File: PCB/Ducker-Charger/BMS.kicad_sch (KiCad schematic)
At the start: 39 parts, among them IC3 BQ34Z100PWR-R2, Q12 BC846, Q13 NCE3080K, Q14 NCE3080K, U8 BQ7791500PWR

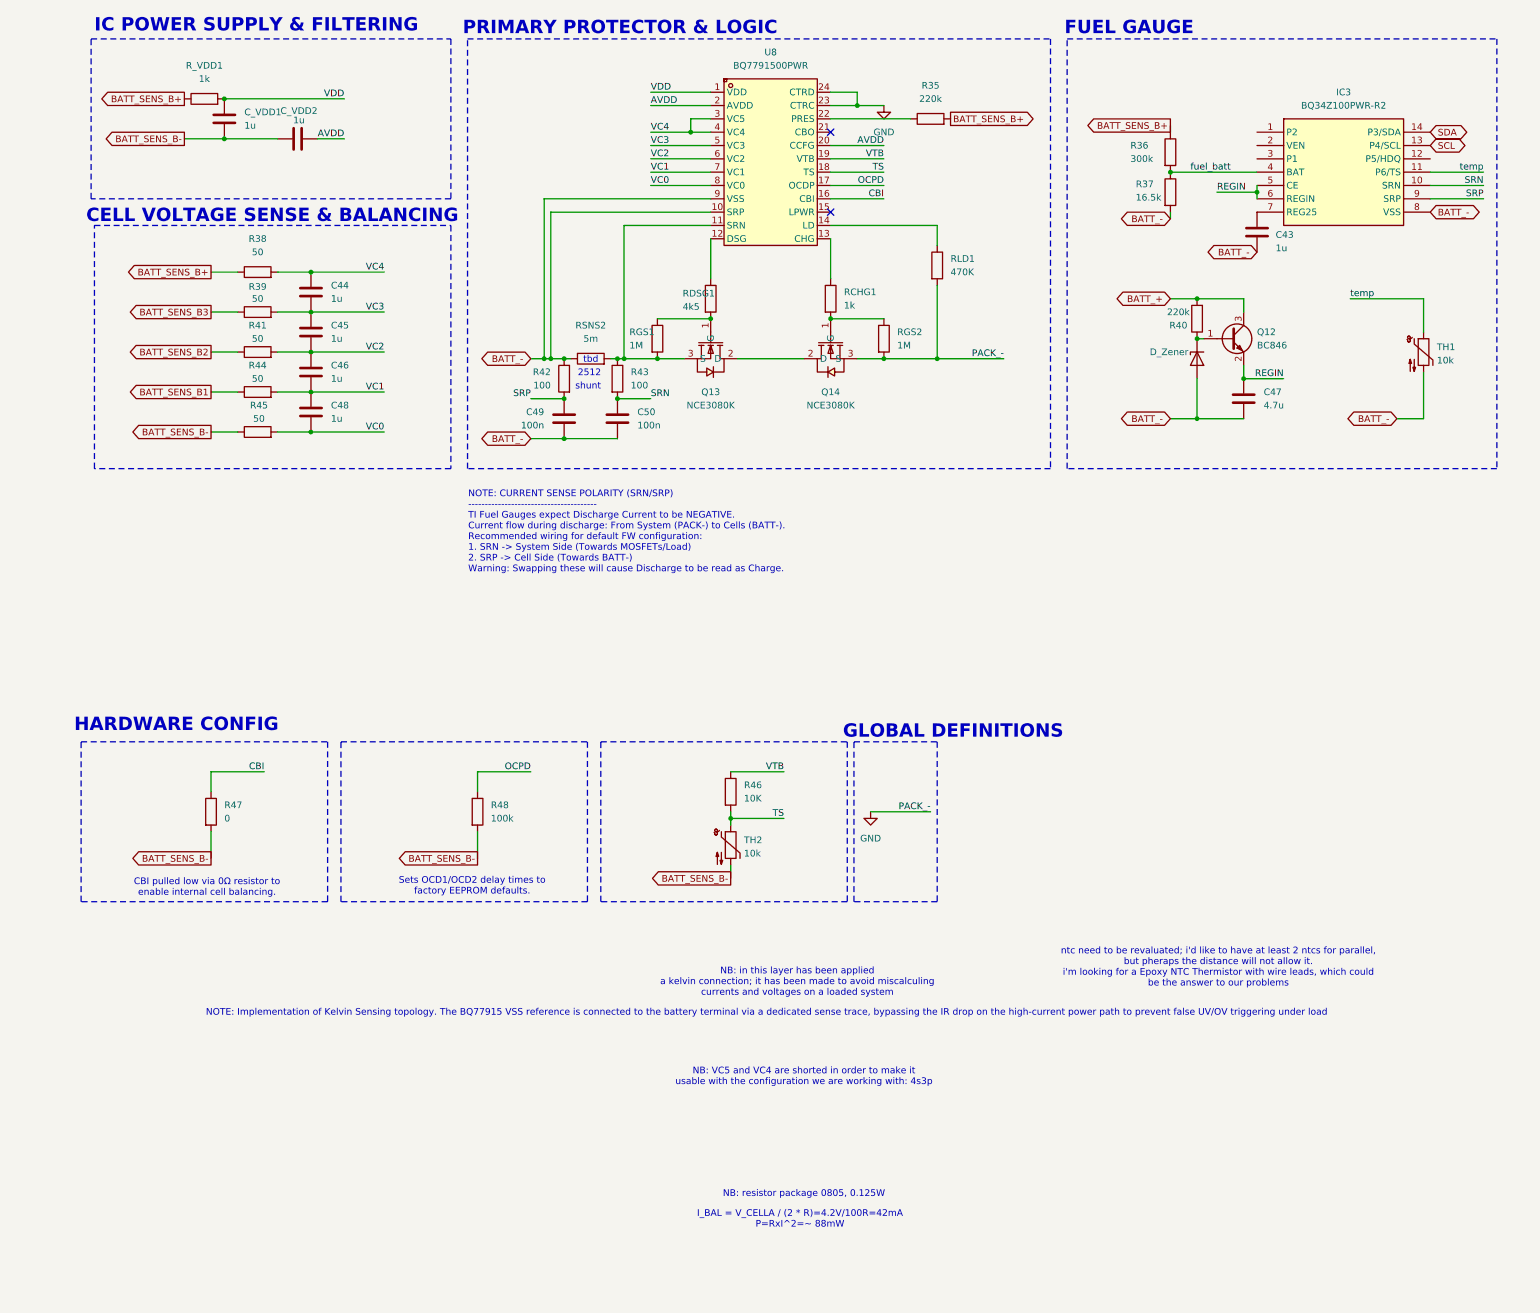
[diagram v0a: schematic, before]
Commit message: fix: power symbols
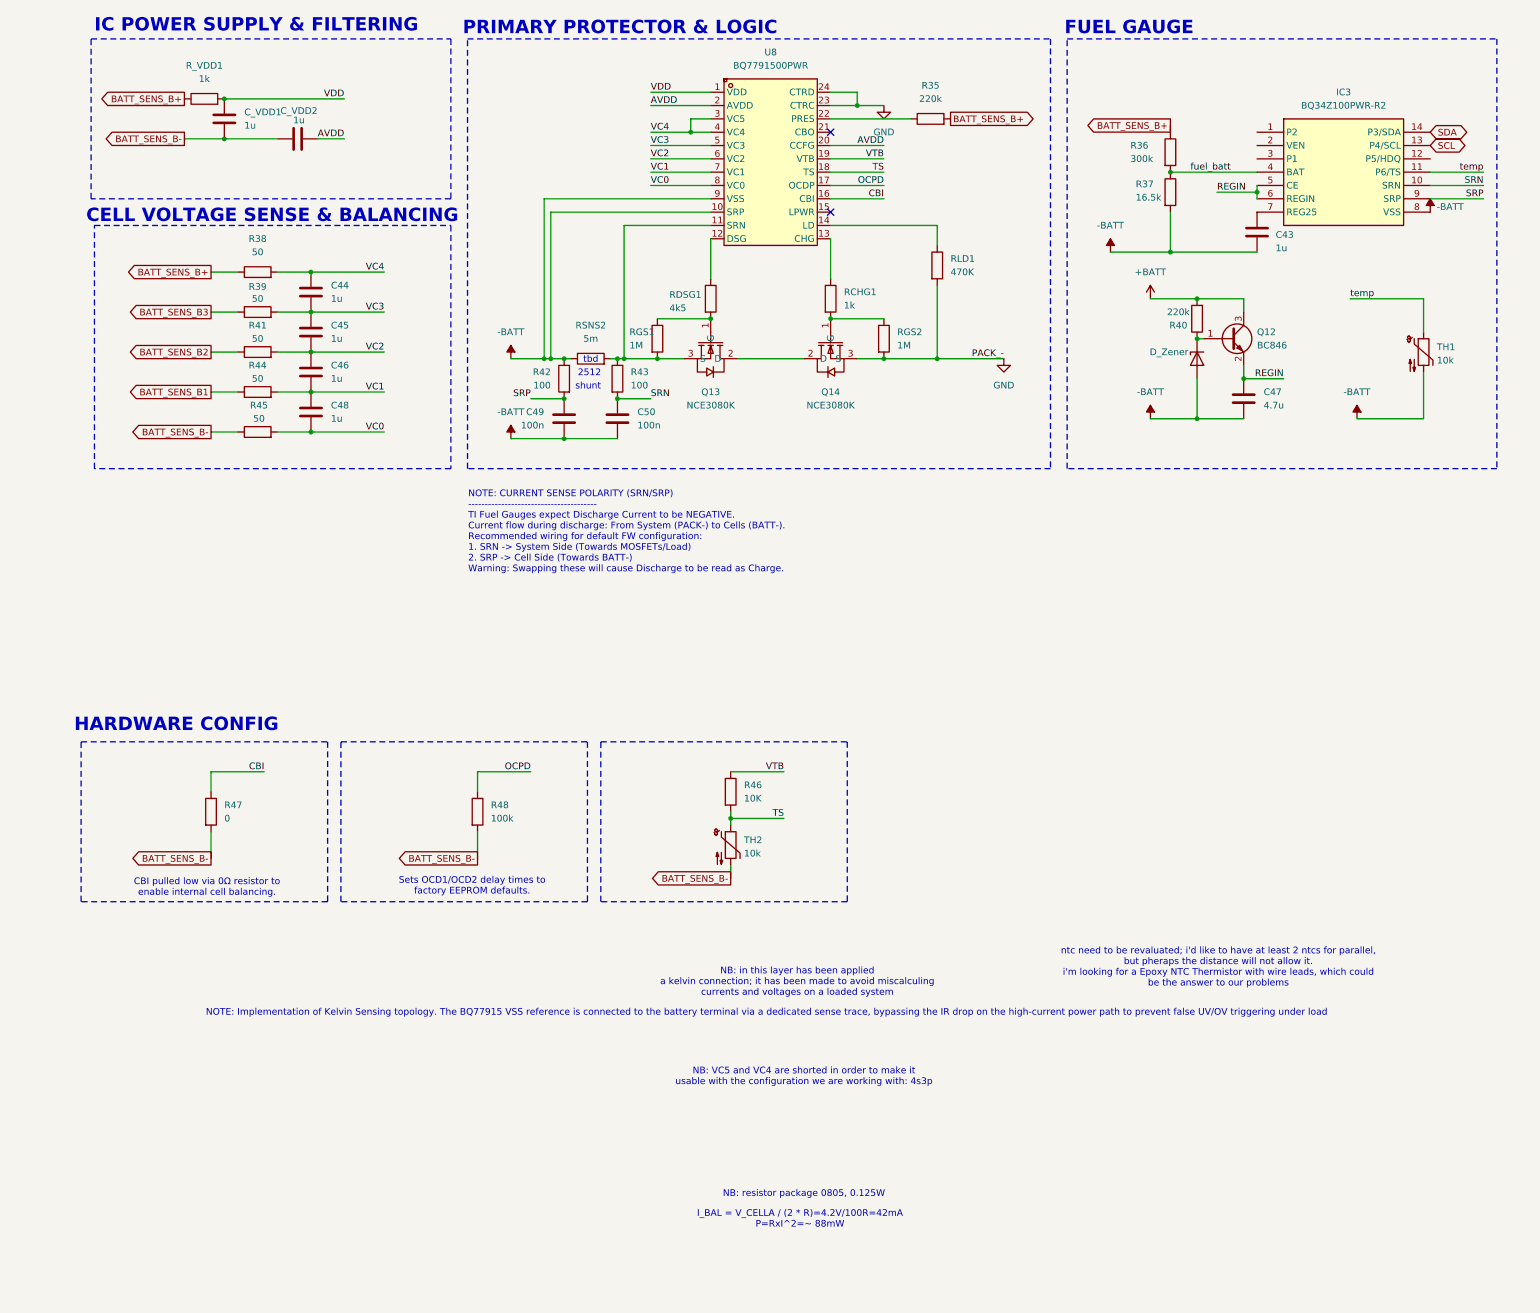
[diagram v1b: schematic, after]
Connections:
- net BATT_+ renamed +BATT
- net BATT_- renamed -BATT
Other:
- note removed: "GLOBAL DEFINITIONS"

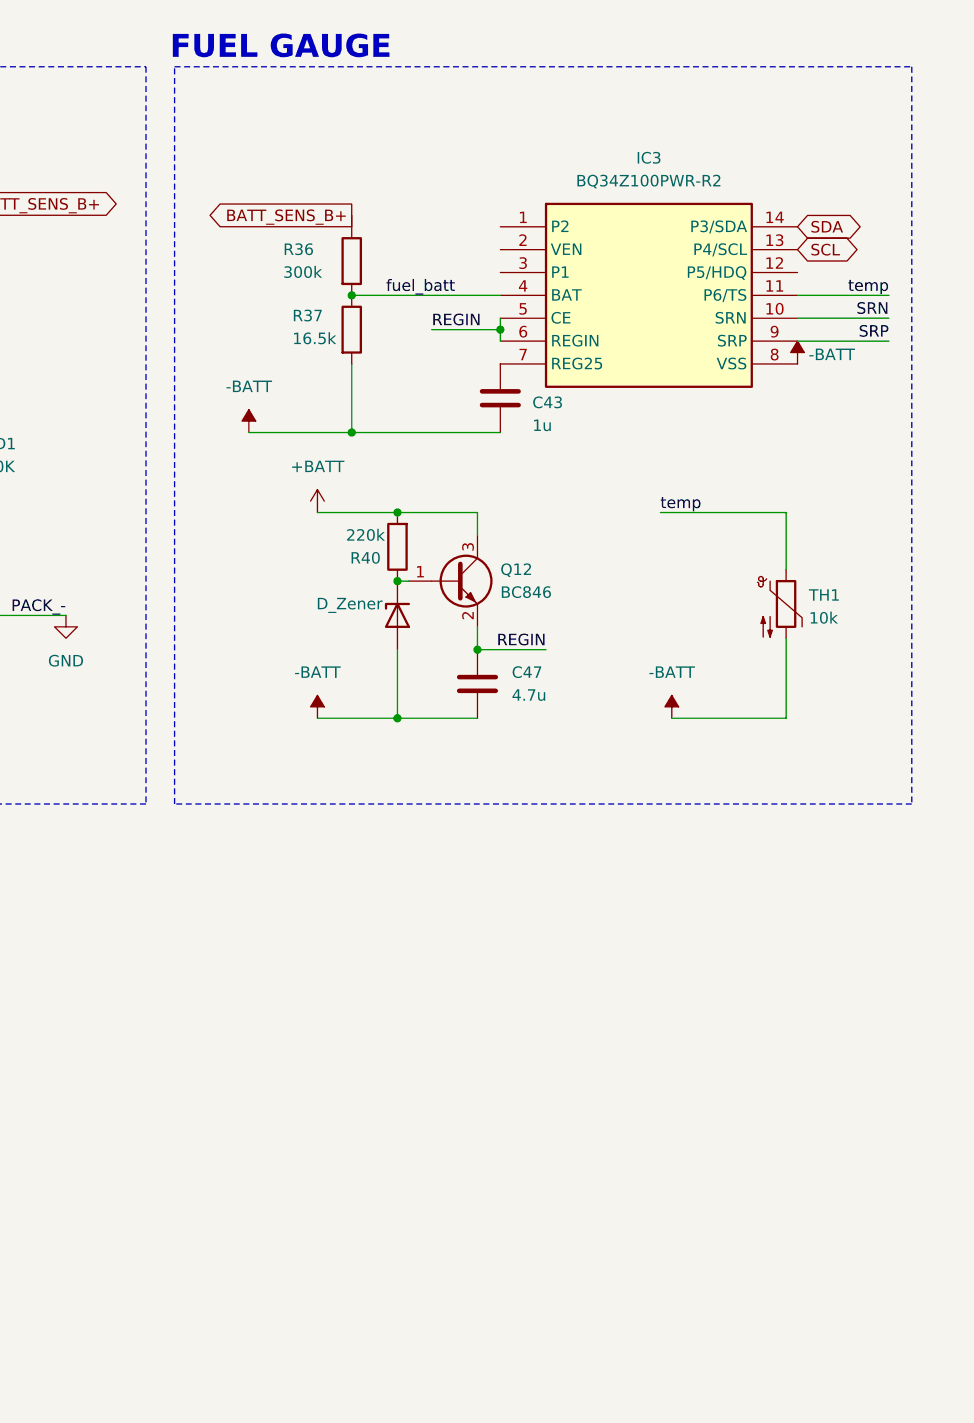
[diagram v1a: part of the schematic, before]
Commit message: fix: I2C is now a BUS, no longer a global label
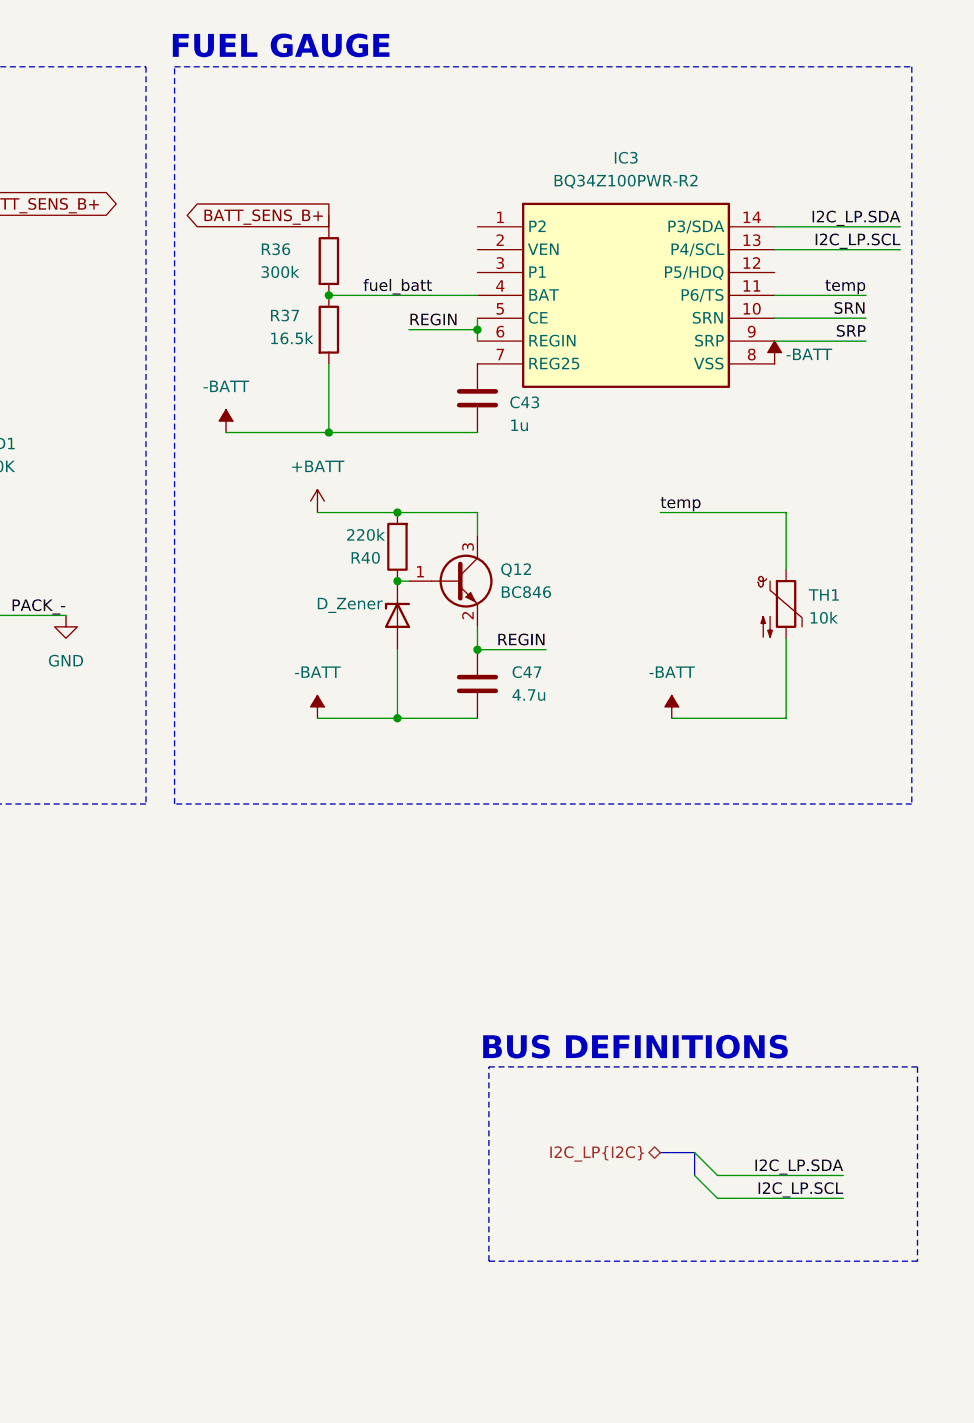
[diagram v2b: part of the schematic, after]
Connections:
- net SCL renamed I2C_LP.SCL
- net SDA renamed I2C_LP.SDA
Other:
- note added: "BUS DEFINITIONS"
- moved on the sheet: C43, IC3, R36, R37

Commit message: feat: added I2C iso IC
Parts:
- removed Q13, Q14: NCE3080K, EasyEDA:TO-252-2_L6.6-W6.1-P4.57-LS9.9-TL-CW, symbol EasyEDA:NCE3080K
- added C54, C55: 100n, symbol Device:C
- added Q1, Q2: BSC040N08NS5, EasyEDA:PG-TDSON-8_L5.9-W5.1-P1.27-LS6.2-BL, symbol EasyEDA:BSC040N08NS5
- added R55, R56: 4k7, symbol Device:R
- added U9: ISO1540DR, EasyEDA:SOIC-8_L4.9-W3.9-P1.27-LS6.0-BL, symbol EasyEDA:ISO1540DR
- R38, R39, R41, R44, R45: value 50 -> 1k
- RSNS2: value 5m -> 2m; footprint (none) -> EasyEDA:R3920
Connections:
- net -BATT: now also C55.2, U9.5 (GND2)
- net GND: now also C54.2, Q2.1 (S), Q2.2 (S), Q2.3 (S), U9.4 (GND1)
- net I2C_LP.SCL: now also U9.3 (SCL1); no longer IC3.13 (P4/SCL)
- net I2C_LP.SDA: now also U9.2 (SDA1); no longer IC3.14 (P3/SDA)
- net REGIN: now also C55.1, R55.1, R56.1, U9.8 (VCC2)
- net at R43.1, RGS1.2, RSNS2.2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: now also Q1.1 (S), Q1.2 (S), Q1.3 (S)
- net at RCHG1.2, RGS2.1: now also Q2.4 (G)
- net at RDSG1.2, RGS1.1: now also Q1.4 (G)
- new net: Q1.5 (D), Q1.6 (D), Q1.7 (D), Q1.8 (D), Q2.5 (D), Q2.6 (D), Q2.7 (D), Q2.8 (D)
- new net +3V3: C54.1, U9.1 (VCC1)
- new net SCL_NOTISO: IC3.13 (P4/SCL), R56.2, U9.6 (SCL2)
- new net SDA_NOTISO: IC3.14 (P3/SDA), R55.2, U9.7 (SDA2)
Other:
- note added: "3920"
- note added: "I2C ISO IC"
- note removed: "2512"
- note removed: "shunt"
- note removed: "tbd"

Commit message: feat: updated footprints
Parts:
- C43, C44, C45, C46, C47, C48, C_VDD1, C_VDD2: footprint (none) -> Capacitor_SMD:C_0805_2012Metric
- C49, C50, C54, C55: footprint (none) -> Capacitor_SMD:C_0603_1608Metric
- D3: footprint (none) -> Diode_SMD:D_SOD-123
- R35, R36, R37, R38, R39, R40, R41, R42, R43, R44, R45, R46, R47, R48, R55, R56, RCHG1, RDSG1, RGS1, RGS2, RLD1, R_VDD1, TH1, TH2: footprint (none) -> Resistor_SMD:R_0603_1608Metric
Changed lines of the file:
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@@
 			)
 		)
-		(property "Footprint" ""
+		(property "Footprint" "Capacitor_SMD:C_0805_2012Metric"
 			(at 58.1152 99.06 0)
 			(effects
@@
 			)
 		)
-		(property "Footprint" ""
+		(property "Footprint" "Resistor_SMD:R_0603_1608Metric"
 			(at 216.662 60.96 90)
 			(effects
@@
 			)
 		)
-		(property "Footprint" ""
+		(property "Footprint" "Capacitor_SMD:C_0603_1608Metric"
 			(at 225.7552 156.21 0)
 			(effects
@@
 			)
 		)
-		(property "Footprint" ""
+		(property "Footprint" "Resistor_SMD:R_0603_1608Metric"
 			(at 269.24 90.17 0)
 			(effects
@@
 			)
 		)
-		(property "Footprint" ""
+		(property "Footprint" "Resistor_SMD:R_0603_1608Metric"
 			(at 46.99 77.978 90)
 			(effects
@@
 			)
 		)
-		(property "Footprint" ""
+		(property "Footprint" "Resistor_SMD:R_0603_1608Metric"
 			(at 164.592 88.9 90)
 			(effects
@@
 			)
 		)
-		(property "Footprint" ""
+		(property "Footprint" "Capacitor_SMD:C_0805_2012Metric"
 			(at 58.1152 106.68 0)
 			(effects
@@
 			)
 		)
-		(property "Footprint" ""
+		(property "Footprint" "Capacitor_SMD:C_0805_2012Metric"
 			(at 58.1152 91.44 0)
 			(effects
@@
 			)
 		)
-		(property "Footprint" ""
+		(property "Footprint" "Resistor_SMD:R_0603_1608Metric"
 			(at 107.188 96.52 90)
 			(effects
@@
 			)
 		)
-		(property "Footprint" ""
+		(property "Footprint" "Resistor_SMD:R_0603_1608Metric"
 			(at 229.362 135.89 90)
 			(effects
@@
 			)
 		)
-		(property "Footprint" ""
+		(property "Footprint" "Resistor_SMD:R_0603_1608Metric"
 			(at 131.572 81.28 90)
 			(effects
@@
 			)
 		)
-		(property "Footprint" ""
+		(property "Footprint" "Resistor_SMD:R_0603_1608Metric"
 			(at 46.99 85.598 90)
 			(effects
@@
 			)
 		)
-		(property "Footprint" ""
+		(property "Footprint" "Capacitor_SMD:C_0805_2012Metric"
 			(at 41.6052 50.8 0)
 			(effects
@@
 			)
 		)
-		(property "Footprint" ""
+		(property "Footprint" "Resistor_SMD:R_0603_1608Metric"
 			(at 137.16 184.15 0)
 			(effects
@@
 			)
 		)
-		(property "Footprint" ""
+		(property "Footprint" "Resistor_SMD:R_0603_1608Metric"
 			(at 46.99 100.838 90)
 			(effects
@@
 			)
 		)
-		(property "Footprint" ""
+		(property "Footprint" "Resistor_SMD:R_0603_1608Metric"
 			(at 36.322 179.07 90)
 			(effects
@@
 			)
 		)
-		(property "Footprint" ""
+		(property "Footprint" "Resistor_SMD:R_0603_1608Metric"
 			(at 174.752 74.93 90)
 			(effects
@@
 			)
 		)
-		(property "Footprint" ""
+		(property "Footprint" "Resistor_SMD:R_0603_1608Metric"
 			(at 220.472 138.43 90)
 			(effects
@@
 			)
 		)
-		(property "Footprint" ""
+		(property "Footprint" "Capacitor_SMD:C_0805_2012Metric"
 			(at 58.42 49.8348 0)
 			(effects
@@
 			)
 		)
-		(property "Footprint" ""
+		(property "Footprint" "Capacitor_SMD:C_0603_1608Metric"
 			(at 104.4448 107.95 0)
 			(effects
@@
 			)
 		)
-		(property "Footprint" ""
+		(property "Footprint" "Resistor_SMD:R_0603_1608Metric"
 			(at 87.122 179.07 90)
 			(effects
@@
 			)
 		)
-		(property "Footprint" ""
+		(property "Footprint" "Resistor_SMD:R_0603_1608Metric"
 			(at 46.99 108.458 90)
 			(effects
@@
 			)
 		)
-		(property "Footprint" ""
+		(property "Footprint" "Resistor_SMD:R_0603_1608Metric"
 			(at 36.83 44.958 90)
 			(effects
@@
 			)
 		)
-		(property "Footprint" ""
+		(property "Footprint" "Resistor_SMD:R_0603_1608Metric"
 			(at 113.792 96.52 90)
 			(effects
@@
 			)
 		)
-		(property "Footprint" ""
+		(property "Footprint" "Resistor_SMD:R_0603_1608Metric"
 			(at 46.99 93.218 90)
 			(effects
@@
 			)
 		)
-		(property "Footprint" ""
+		(property "Footprint" "Resistor_SMD:R_0603_1608Metric"
 			(at 227.838 85.09 90)
 			(effects
@@
 			)
 		)
-		(property "Footprint" ""
+		(property "Footprint" "Capacitor_SMD:C_0805_2012Metric"
 			(at 58.1152 83.82 0)
 			(effects
@@
 			)
 		)
-		(property "Footprint" ""
+		(property "Footprint" "Capacitor_SMD:C_0603_1608Metric"
 			(at 213.0552 156.21 0)
 			(effects
@@
 			)
 		)
-		(property "Footprint" ""
+		(property "Footprint" "Resistor_SMD:R_0603_1608Metric"
 			(at 135.382 175.26 90)
 			(effects
@@
 			)
 		)
-		(property "Footprint" ""
+		(property "Footprint" "Capacitor_SMD:C_0805_2012Metric"
 			(at 235.9152 72.39 0)
 			(effects
@@
 			)
 		)
-		(property "Footprint" ""
+		(property "Footprint" "Capacitor_SMD:C_0805_2012Metric"
 			(at 235.9152 104.14 0)
 			(effects
@@
 			)
 		)
-		(property "Footprint" ""
+		(property "Footprint" "Diode_SMD:D_SOD-123"
 			(at 226.06 92.71 0)
 			(effects
@@
 			)
 		)
-		(property "Footprint" ""
+		(property "Footprint" "Resistor_SMD:R_0603_1608Metric"
 			(at 175.26 48.768 90)
 			(effects
@@
 			)
 		)
-		(property "Footprint" ""
+		(property "Footprint" "Resistor_SMD:R_0603_1608Metric"
 			(at 154.432 81.28 90)
 			(effects
@@
 			)
 		)
-		(property "Footprint" ""
+		(property "Footprint" "Resistor_SMD:R_0603_1608Metric"
 			(at 216.662 53.34 90)
 			(effects
@@
 			)
 		)
-		(property "Footprint" ""
+		(property "Footprint" "Resistor_SMD:R_0603_1608Metric"
 			(at 121.412 88.9 90)
 			(effects
@@
 			)
 		)
-		(property "Footprint" ""
+		(property "Footprint" "Capacitor_SMD:C_0603_1608Metric"
 			(at 116.5352 107.95 0)
 			(effects
